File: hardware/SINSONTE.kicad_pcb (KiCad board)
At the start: 2 copper layers, 9 parts, among them J1 Conn_01x02_Male, J2 Conn_01x02_Male, Q1 2N7000, U1 Pico

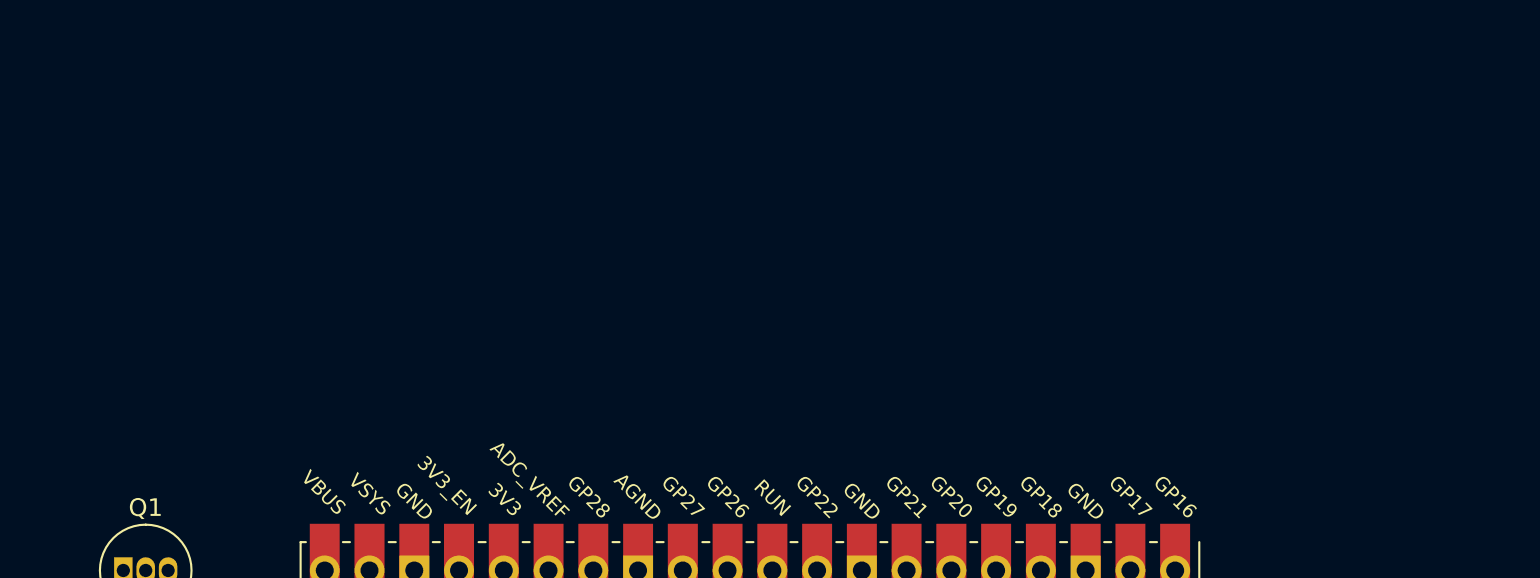
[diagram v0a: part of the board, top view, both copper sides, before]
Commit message: core components added
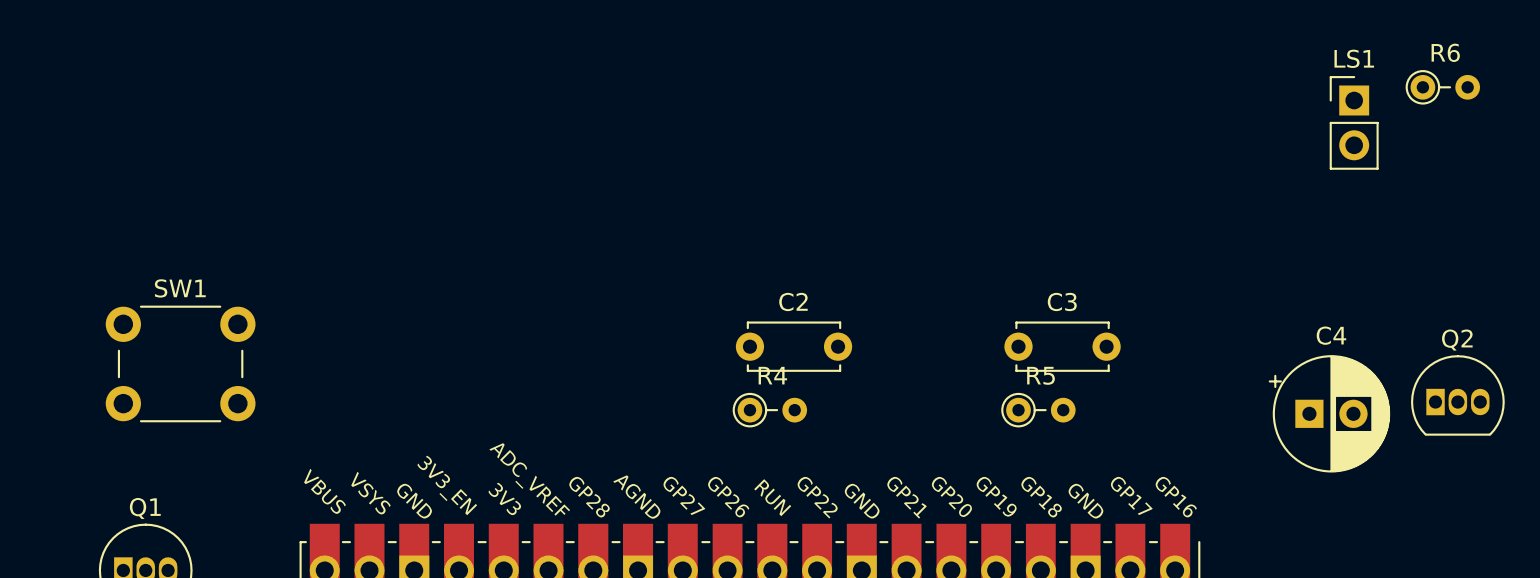
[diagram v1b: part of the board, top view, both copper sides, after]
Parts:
- added C2: C, Capacitor_THT:C_Disc_D5.0mm_W2.5mm_P5.00mm, F.Cu at (200.7, 54.6)
- added C3: C, Capacitor_THT:C_Disc_D5.0mm_W2.5mm_P5.00mm, F.Cu at (215.9, 54.6)
- added C4: CP, Capacitor_THT:CP_Radial_D6.3mm_P2.50mm, F.Cu at (232.4, 58.4)
- added LS1: Speaker, Connector_PinHeader_2.54mm:PinHeader_1x02_P2.54mm_Vertical, F.Cu at (234.9, 40.6)
- added Q2: PN2222A, Package_TO_SOT_THT:TO-92_Inline, F.Cu at (239.6, 57.8)
- added R4: R, Resistor_THT:R_Axial_DIN0204_L3.6mm_D1.6mm_P2.54mm_Vertical, F.Cu at (200.7, 58.2)
- added R5: R, Resistor_THT:R_Axial_DIN0204_L3.6mm_D1.6mm_P2.54mm_Vertical, F.Cu at (215.9, 58.2)
- added R6: R, Resistor_THT:R_Axial_DIN0204_L3.6mm_D1.6mm_P2.54mm_Vertical, F.Cu at (238.8, 39.9)
- added SW1: SW_Push, Button_Switch_THT:SW_PUSH_6mm_H4.3mm, F.Cu at (165.1, 53.3)
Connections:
- C1 pad 2: Net-(C1-Pad2) -> Net-(BT1-Pad2)
- J2 pad 1: Net-(J2-Pad1) -> Net-(BT1-Pad1)
- J2 pad 2: Net-(J2-Pad2) -> Net-(C1-Pad1)
- Q1 pad 1: Net-(Q1-Pad1) -> Net-(BT1-Pad2)
- R1 pad 1: Net-(R1-Pad1) -> Net-(Q1-Pad2)
- R1 pad 2: Net-(R1-Pad2) -> Net-(BT1-Pad2)
- R2 pad 2: Net-(R2-Pad2) -> Net-(Q1-Pad2)
- R3 pad 1: Net-(R3-Pad1) -> Net-(C1-Pad1)
- R3 pad 2: Net-(R3-Pad2) -> Net-(Q1-Pad2)
- U1 pad 29: Net-(U1-Pad29) -> Net-(R2-Pad1)
- U1 pad 3: Net-(BT1-Pad2) -> Net-(Q1-Pad3)

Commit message: updated features elements added
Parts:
- added J3: LIGHT_SENSOR, Connector_PinHeader_2.54mm:PinHeader_1x02_P2.54mm_Vertical, F.Cu at (191.8, 39.4)
- added JP1: 12H - 24H, Jumper:SolderJumper-3_P1.3mm_Open_RoundedPad1.0x1.5mm_NumberLabels, F.Cu at (219.7, 36.8)
- added R7: R, Resistor_THT:R_Axial_DIN0204_L3.6mm_D1.6mm_P2.54mm_Vertical, F.Cu at (195.7, 38.6)
- added R8: R, Resistor_THT:R_Axial_DIN0204_L3.6mm_D1.6mm_P2.54mm_Vertical, F.Cu at (218.5, 40.2)
- J1: value Conn_01x02_Male -> BAT
- J2: value Conn_01x02_Male -> CLOCK
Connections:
- C2 pad 2: Net-(BT1-Pad2) -> Net-(C2-Pad2)
- C3 pad 2: Net-(BT1-Pad2) -> Net-(C2-Pad2)
- Q1 pad 3: Net-(Q1-Pad3) -> Net-(C2-Pad2)
- Q2 pad 1: Net-(BT1-Pad2) -> Net-(C2-Pad2)
- U1 pad 3: Net-(Q1-Pad3) -> Net-(C2-Pad2)

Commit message: 90% routed
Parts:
- removed C3: C, Capacitor_THT:C_Disc_D5.0mm_W2.5mm_P5.00mm
- removed R5: R, Resistor_THT:R_Axial_DIN0204_L3.6mm_D1.6mm_P2.54mm_Vertical
- JP1: moved to B.Cu
- moved JP1 138.3 mm to (85.1, 68.6), turned to 270 degrees
- moved R4 134.7 mm to (66.0, 54.6)
- moved Q2 131.6 mm to (108.0, 57.1)
- moved C4 129.6 mm to (102.9, 53.6), turned to 180 degrees
- moved C2 129.5 mm to (71.1, 54.6)
- moved R6 128.9 mm to (110.5, 52.1), turned to 180 degrees
- moved U1 122.9 mm to (78.0, 69.0)
- moved R8 118.0 mm to (106.7, 78.1)
- moved J1 117.4 mm to (52.1, 99.1), turned to 0 degrees
- moved BT1 113.4 mm to (57.0, 92.7)
- moved LS1 101.0 mm to (134.6, 52.1), turned to 90 degrees
- moved R7 95.2 mm to (106.7, 72.4)
- moved J3 88.4 mm to (108.0, 67.3), turned to 180 degrees
- moved Q1 62.2 mm to (117.5, 107.3), turned to 90 degrees
- moved SW1 53.4 mm to (127.6, 91.4), turned to 270 degrees
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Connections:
- C4 pad 2: Net-(C3-Pad1) -> Net-(C2-Pad1)
- JP1 pad 3: Net-(C2-Pad2) -> Net-(JP1-Pad3)
- Q1 pad 3: Net-(C2-Pad2) -> Net-(JP1-Pad3)
- R6 pad 1: Net-(BT1-Pad1) -> Net-(LS1-Pad2)
- U1 pad 18: Net-(U1-Pad18) -> Net-(JP1-Pad3)
- U1 pad 19: Net-(U1-Pad19) -> Net-(R2-Pad1)
- U1 pad 20: Net-(U1-Pad20) -> Net-(R8-Pad1)
- U1 pad 24: Net-(R8-Pad1) -> Net-(U1-Pad24)
- U1 pad 29: Net-(R2-Pad1) -> Net-(U1-Pad29)
- U1 pad 3: Net-(C2-Pad2) -> Net-(U1-Pad3)
- U1 pad 38: Net-(U1-Pad38) -> Net-(C2-Pad2)
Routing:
- net Net-(BT1-Pad2): track 0.00 -> 93.1 mm
- net Net-(BT1-Pad1): track 0.00 -> 59.8 mm
- net Net-(JP1-Pad3): track 0.00 -> 54.9 mm
- net Net-(JP1-Pad1): track 0.00 -> 49.1 mm
- net Net-(C1-Pad1): track 0.00 -> 48.1 mm
- net Net-(J3-Pad1): track 0.00 -> 42.0 mm
- net Net-(C2-Pad1): track 0.00 -> 33.3 mm
- net Net-(JP1-Pad2): track 0.00 -> 28.7 mm
- net Net-(R2-Pad1): track 0.00 -> 28.3 mm
- net Net-(C2-Pad2): track 0.00 -> 25.7 mm
- net Net-(Q1-Pad2): track 0.00 -> 24.0 mm
- net Net-(R4-Pad1): track 0.00 -> 7.52 mm
- net Net-(R8-Pad1): track 0.00 -> 4.64 mm
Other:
- board outline added: 90 x 70 mm

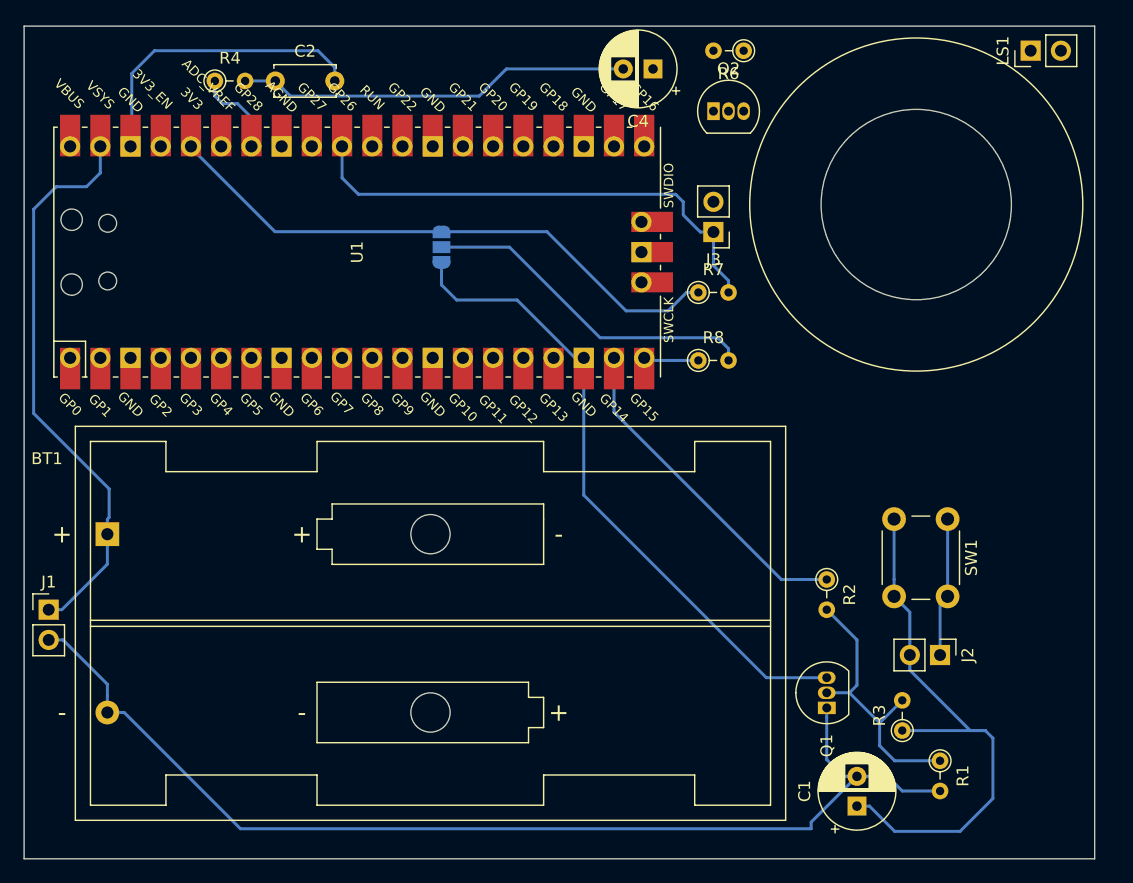
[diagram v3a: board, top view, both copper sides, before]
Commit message: all traces routed
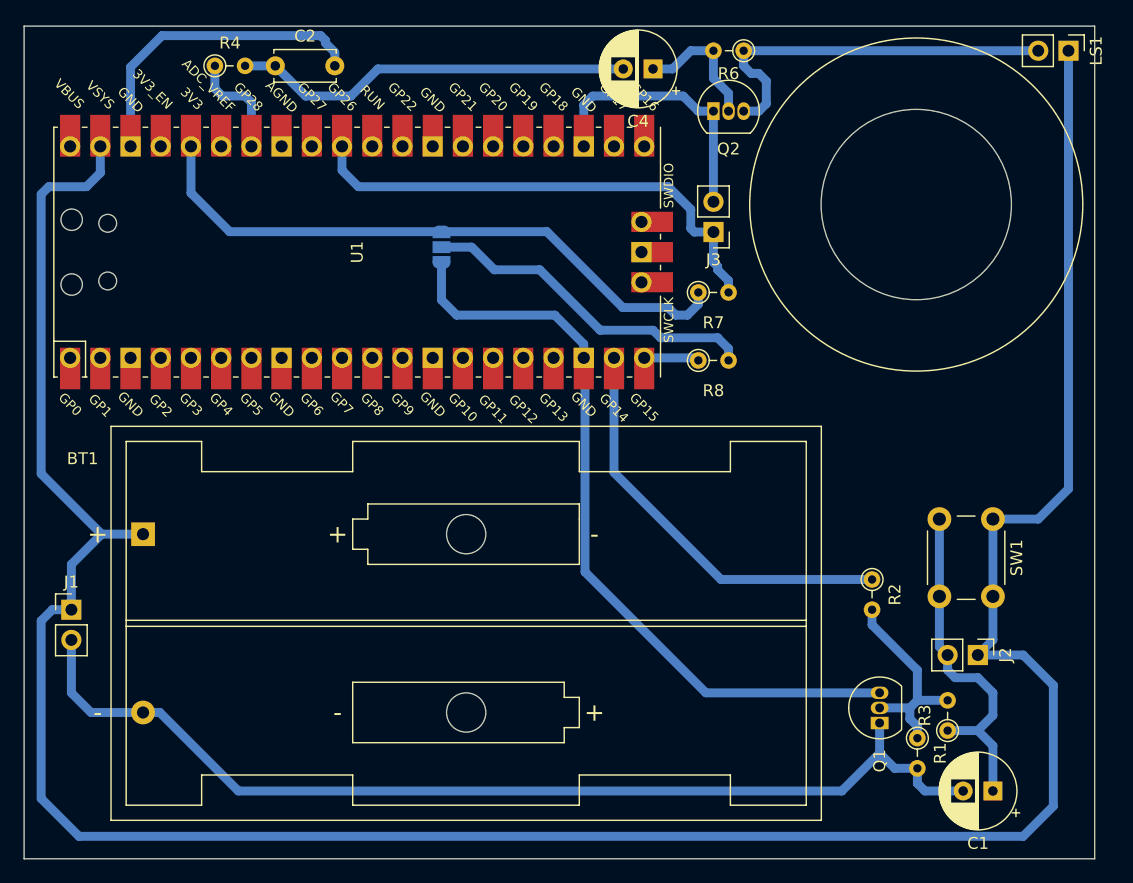
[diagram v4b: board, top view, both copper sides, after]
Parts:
- moved C1 11.5 mm to (131.4, 114.3), turned to 180 degrees
- moved Q1 4.62 mm to (121.9, 108.6)
- moved R2 3.81 mm to (121.3, 96.5)
- moved R3 3.81 mm to (127.6, 109.2)
- moved SW1 3.81 mm to (131.4, 91.4)
- moved J2 3.18 mm to (130.2, 102.9)
- moved LS1 3.17 mm to (137.8, 52.1), turned to 270 degrees
- moved BT1 3.00 mm to (60.0, 92.7)
- moved R1 2.69 mm to (125.1, 109.9)
- moved J1 1.91 mm to (54.0, 99.1)
- moved C2 1.27 mm to (71.1, 53.3)
- moved R4 1.27 mm to (66.0, 53.3)
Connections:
- J3 pad 2: Net-(C2-Pad2) -> Net-(J3-Pad2)
- Q2 pad 1: Net-(C2-Pad2) -> Net-(J3-Pad2)
- U1 pad 23: Net-(U1-Pad23) -> Net-(J3-Pad2)
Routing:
- net Net-(BT1-Pad1): track 59.8 -> 228.6 mm
- net Net-(LS1-Pad2): track 0.00 -> 32.5 mm
- net Net-(J3-Pad2): track 0.00 -> 22.8 mm
- net Net-(C1-Pad1): track 48.1 -> 29.4 mm
- net Net-(JP1-Pad3): track 54.9 -> 66.4 mm
- net Net-(C4-Pad1): track 0.00 -> 11.3 mm
- net Net-(R2-Pad1): track 28.3 -> 35.1 mm
- net Net-(Q1-Pad2): track 24.0 -> 18.0 mm
- net Net-(BT1-Pad2): track 93.1 -> 88.7 mm
- net Net-(JP1-Pad1): track 49.1 -> 52.3 mm
- net Net-(R4-Pad1): track 7.52 -> 9.16 mm
- net Net-(C2-Pad2): track 25.7 -> 26.9 mm
- net Net-(C2-Pad1): track 33.3 -> 33.8 mm
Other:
- net class Default: trace_width 0.25 -> 0.75

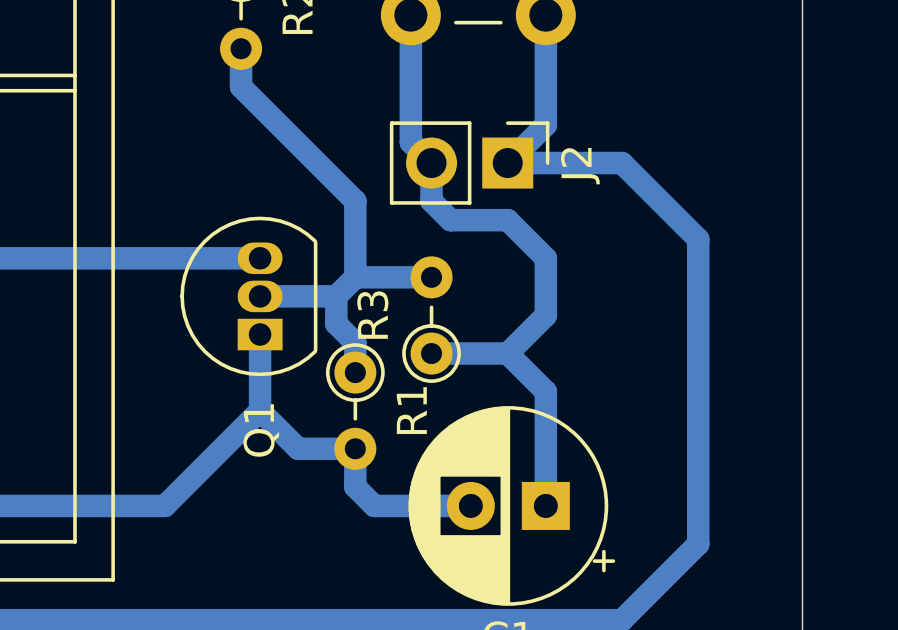
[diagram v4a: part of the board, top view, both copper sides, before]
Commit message: resistor removed
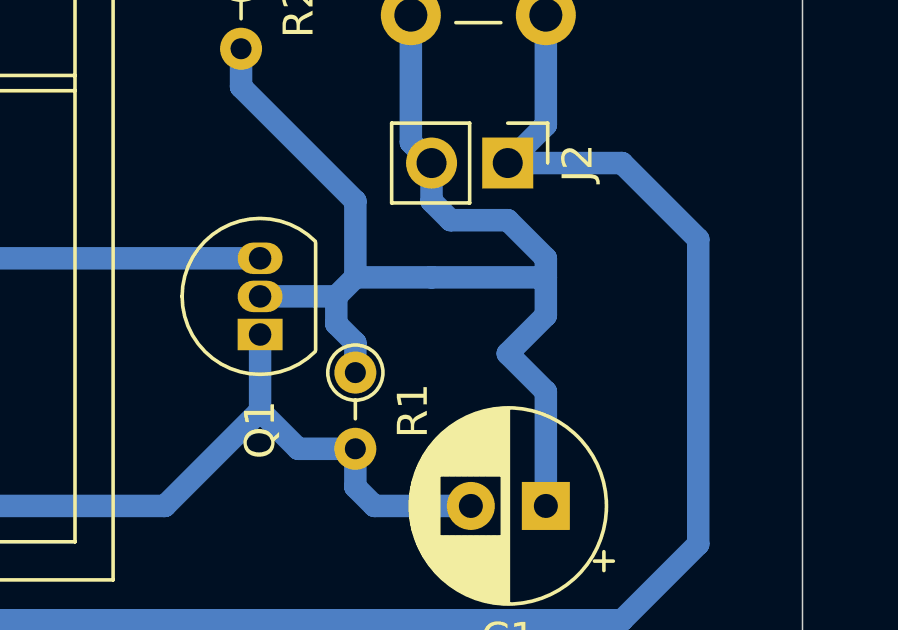
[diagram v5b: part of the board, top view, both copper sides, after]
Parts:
- removed R3: R, Resistor_THT:R_Axial_DIN0204_L3.6mm_D1.6mm_P2.54mm_Vertical
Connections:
- Q1 pad 2: Net-(Q1-Pad2) -> Net-(C1-Pad1)
- R1 pad 1: Net-(Q1-Pad2) -> Net-(C1-Pad1)
- R2 pad 2: Net-(Q1-Pad2) -> Net-(C1-Pad1)
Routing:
- net Net-(C1-Pad1): track 29.4 -> 48.7 mm
- net Net-(Q1-Pad2): track 18.0 -> 0.00 mm

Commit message: expansion headers
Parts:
- added J4: Conn_01x17_Male, Connector_PinHeader_2.54mm:PinHeader_1x17_P2.54mm_Vertical, F.Cu at (53.9, 80.4)
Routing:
- net Net-(J4-Pad9): track 0.00 -> 2.54 mm
- net Net-(J4-Pad8): track 0.00 -> 2.54 mm
- net Net-(J4-Pad7): track 0.00 -> 2.54 mm
- net Net-(J4-Pad6): track 0.00 -> 2.54 mm
- net Net-(J4-Pad5): track 0.00 -> 2.54 mm
- net Net-(J4-Pad4): track 0.00 -> 2.54 mm
- net Net-(J4-Pad3): track 0.00 -> 2.54 mm
- net Net-(J4-Pad2): track 0.00 -> 2.54 mm
- net Net-(J4-Pad17): track 0.00 -> 2.54 mm
- net Net-(J4-Pad16): track 0.00 -> 2.54 mm
- net Net-(J4-Pad15): track 0.00 -> 2.54 mm
- net Net-(J4-Pad14): track 0.00 -> 2.54 mm
- net Net-(J4-Pad13): track 0.00 -> 2.54 mm
- net Net-(J4-Pad12): track 0.00 -> 2.54 mm
- net Net-(J4-Pad11): track 0.00 -> 2.54 mm
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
